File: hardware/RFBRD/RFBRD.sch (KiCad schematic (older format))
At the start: 0 parts

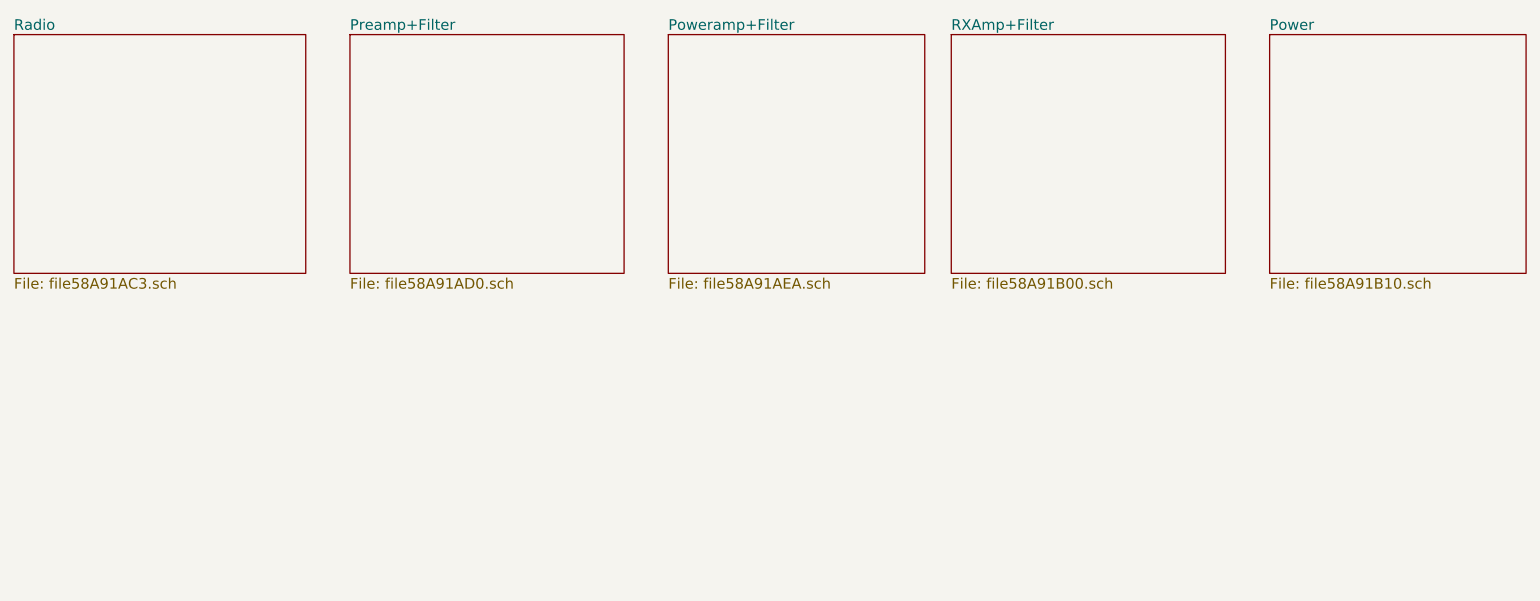
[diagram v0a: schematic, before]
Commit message: Added bits of the RF Board, dumped to PCB.
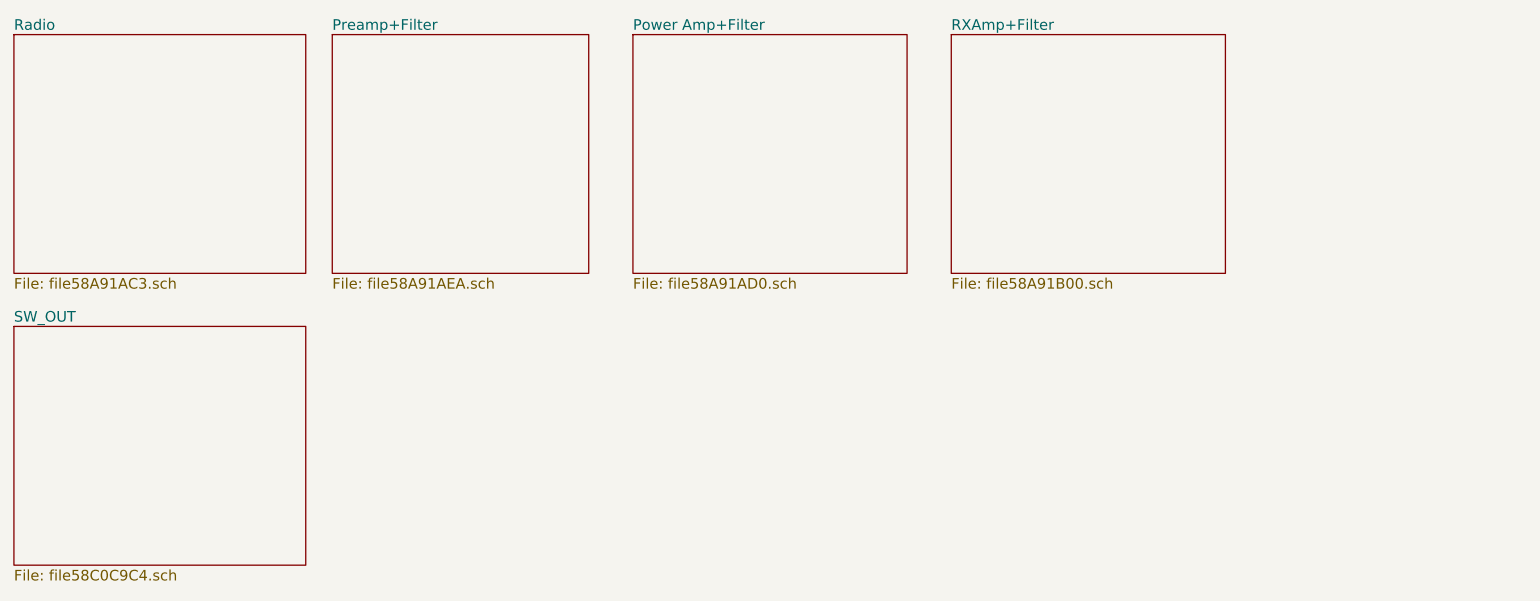
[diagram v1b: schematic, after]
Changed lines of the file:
@@
 LIBS:contrib
 LIBS:valves
+LIBS:RFT
+LIBS:RFBRD-cache
 EELAYER 25 0
 EELAYER END
@@
 $EndSheet
 $Sheet
-S 2600 700  1550 1350
+S 4200 700  1550 1350
 U 58A91AD1
-F0 "Preamp+Filter" 60
+F0 "Power Amp+Filter" 60
 F1 "file58A91AD0.sch" 60
 $EndSheet
 $Sheet
-S 4400 700  1450 1350
+S 2500 700  1450 1350
 U 58A91AEB
-F0 "Poweramp+Filter" 60
+F0 "Preamp+Filter" 60
 F1 "file58A91AEA.sch" 60
 $EndSheet
@@
 $EndSheet
 $Sheet
-S 7800 700  1450 1350
-U 58A91B11
-F0 "Power" 60
-F1 "file58A91B10.sch" 60
+S 700  2350 1650 1350
+U 58C0C9C5
+F0 "SW_OUT" 60
+F1 "file58C0C9C4.sch" 60
 $EndSheet
 $EndSCHEMATC
